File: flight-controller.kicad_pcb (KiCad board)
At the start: 2 copper layers, 36 x 36 mm, 9 parts, among them J1 USB_C_Receptacle_USB2.0, U1 AT32F435RGT7, U2 BMI270, U3 BMP280, U4 W25N01GVZEIG, U5 AT7456E, U6 TPS54335A, U7 TPS54335A, U8 TLV75733PDBV

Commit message: Finish majority of MCU pin mapping
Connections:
- U1 pad 10: unconnected-(U1-PC2-Pad10) -> TMR20_CH2
- U1 pad 20: unconnected-(U1-PA4-Pad20) -> SPI1_CS
- U1 pad 24: unconnected-(U1-PC4-Pad24) -> TMR9_CH1
- U1 pad 25: unconnected-(U1-PC5-Pad25) -> TMR9_CH2
- U1 pad 26: unconnected-(U1-PB0-Pad26) -> SPI1_INT
- U1 pad 29: unconnected-(U1-PB10-Pad29) -> TMR2_CH3
- U1 pad 30: unconnected-(U1-PB11-Pad30) -> TMR2_CH4
- U1 pad 33: unconnected-(U1-PB12-Pad33) -> SPI2_CS
- U1 pad 37: unconnected-(U1-PC6-Pad37) -> TIM3_CH1
- U1 pad 38: unconnected-(U1-PC7-Pad38) -> TIM3_CH2
- U1 pad 39: unconnected-(U1-PC8-Pad39) -> TIM3_CH3
- U1 pad 40: unconnected-(U1-PC9-Pad40) -> TIM3_CH4
- U1 pad 54: unconnected-(U1-PD2-Pad54) -> SPI3_CS
- U1 pad 58: unconnected-(U1-PB6-Pad58) -> SPI4_CS
- U1 pad 8: unconnected-(U1-PC0-Pad8) -> I2C3_SCL
- U1 pad 9: unconnected-(U1-PC1-Pad9) -> I2C3_SDA
- U2 pad 12: unconnected-(U2-CSB-Pad12) -> SPI1_CS
- U2 pad 4: unconnected-(U2-INT1-Pad4) -> SPI1_INT
- U3 pad 2: unconnected-(U3-CSB-Pad2) -> SPI2_CS
- U4 pad 1: unconnected-(U4-~{CS}-Pad1) -> SPI3_CS
- U4 pad 4: unconnected-(U4-GND-Pad4) -> GND
- U4 pad 8: unconnected-(U4-VCC-Pad8) -> +3V3
- U4 pad 9: unconnected-(U4-EP-Pad9) -> GND
- U5 pad 20: unconnected-(U5-AGND-Pad20) -> GND
- U5 pad 21: unconnected-(U5-AVDD-Pad21) -> +5V
- U5 pad 23: unconnected-(U5-PGND-Pad23) -> GND
- U5 pad 24: unconnected-(U5-PVDD-Pad24) -> +5V
- U5 pad 27: unconnected-(U5-EP-Pad27) -> GND
- U5 pad 3: unconnected-(U5-DVDD-Pad3) -> +5V
- U5 pad 4: unconnected-(U5-DGND-Pad4) -> GND
- U5 pad 8: unconnected-(U5-~{CS}-Pad8) -> SPI4_CS
- U8 pad 1: unconnected-(U8-IN-Pad1) -> +5V
- U8 pad 2: unconnected-(U8-GND-Pad2) -> GND
- U8 pad 5: unconnected-(U8-OUT-Pad5) -> +3V3

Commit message: Update pcb to match minor schematic change
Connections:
- U1 pad 10: TMR20_CH2 -> unconnected-(U1-PC2-Pad10)
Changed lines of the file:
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@@
   (net 44 "unconnected-(U1-PH1-Pad6)")
   (net 45 "NRST")
-  (net 46 "TMR20_CH2")
+  (net 46 "unconnected-(U1-PC2-Pad10)")
   (net 47 "TMR9_CH1")
   (net 48 "TMR9_CH2")
@@
       (net 38 "I2C3_SDA") (pinfunction "PC1") (pintype "unspecified"))
     (pad "10" smd roundrect (at -5.675 0.75) (size 1.55 0.3) (layers "F.Cu" "F.Paste" "F.Mask") (roundrect_rratio 0.25)
-      (net 46 "TMR20_CH2") (pinfunction "PC2") (pintype "unspecified"))
+      (net 46 "unconnected-(U1-PC2-Pad10)") (pinfunction "PC2") (pintype "unspecified"))
     (pad "11" smd roundrect (at -5.675 1.25) (size 1.55 0.3) (layers "F.Cu" "F.Paste" "F.Mask") (roundrect_rratio 0.25)
       (net 49 "unconnected-(U1-PC3-Pad11)") (pinfunction "PC3") (pintype "unspecified"))

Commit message: Add buzzer and power supply designs for consideration
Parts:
- added U9: USBLC6-2P6, Package_TO_SOT_SMD:SOT-666, F.Cu at (109.8, 100.6)
- U6, U7: value TPS54335A -> TPS54302; footprint Package_SO:TI_SO-PowerPAD-8_ThermalVias -> Package_TO_SOT_SMD:SOT-23-6
- moved U7 3.03 mm to (105.2, 105.6)
- moved U6 2.71 mm to (105.2, 101.2)
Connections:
- net Net-(J1-VBUS-PadA4) renamed VBUS
- J1 pad A6: USB_DP -> EUSB_DP
- J1 pad A7: USB_DM -> EUSB_DM
- J1 pad B6: USB_DP -> EUSB_DP
- J1 pad B7: USB_DM -> EUSB_DM
- U2 pad 2: unconnected-(U2-ASDx-Pad2) -> +3V3
- U2 pad 3: unconnected-(U2-ASCx-Pad3) -> +3V3
- U6 pad 1: unconnected-(U6-BOOT-Pad1) -> GND
- U6 pad 2: unconnected-(U6-VIN-Pad2) -> Net-(U6-SW)
- U6 pad 3: unconnected-(U6-PH-Pad3) -> +BATT
- U6 pad 4: unconnected-(U6-GND-Pad4) -> Net-(U6-FB)
- U6 pad 6: unconnected-(U6-COMP-Pad6) -> Net-(U6-BOOT)
- U7 pad 1: unconnected-(U7-BOOT-Pad1) -> GND
- U7 pad 2: unconnected-(U7-VIN-Pad2) -> Net-(U7-SW)
- U7 pad 3: unconnected-(U7-PH-Pad3) -> +BATT
- U7 pad 4: unconnected-(U7-GND-Pad4) -> Net-(U7-FB)
- U7 pad 5: unconnected-(U7-VSENSE-Pad5) -> 10V_SW
- U7 pad 6: unconnected-(U7-COMP-Pad6) -> Net-(U7-BOOT)
- U8 pad 3: unconnected-(U8-EN-Pad3) -> +5V

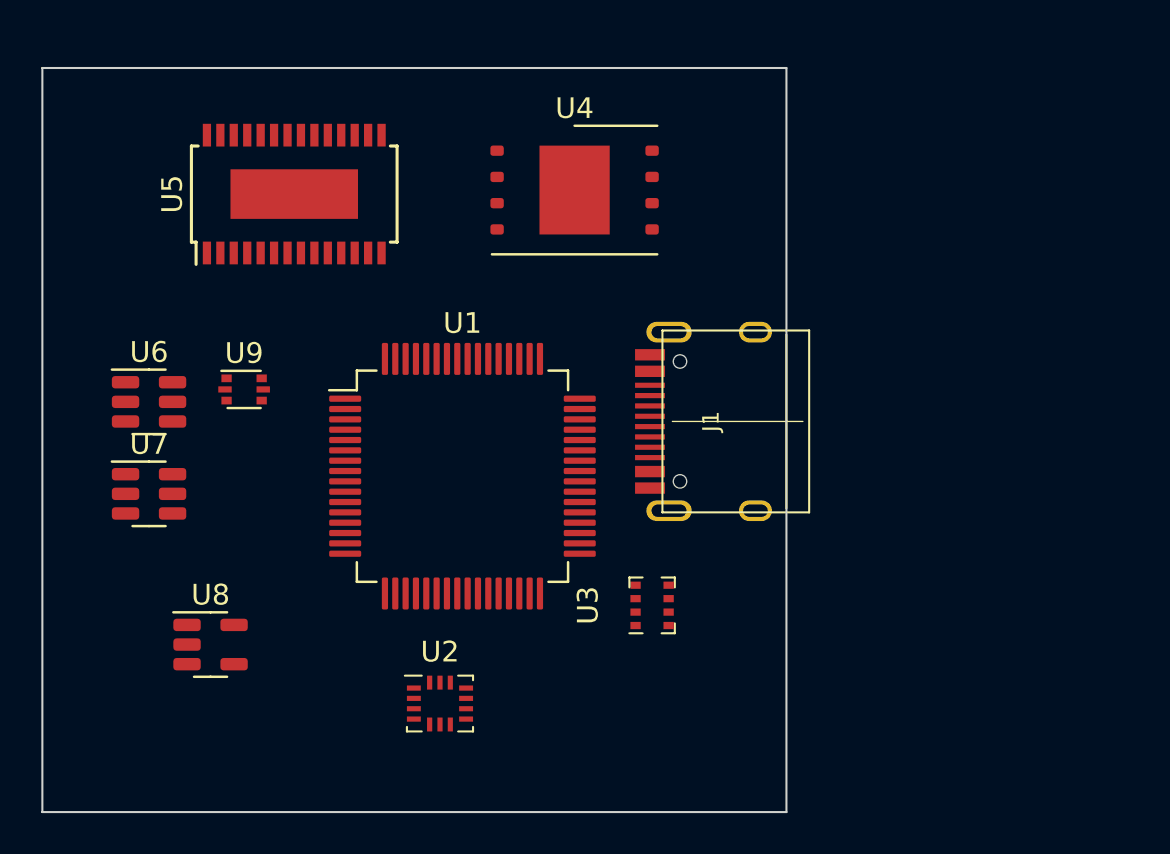
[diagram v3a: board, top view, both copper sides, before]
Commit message: Add LCSC part numbers for major parts. Provisionally delect power supply capacitors and inductors.
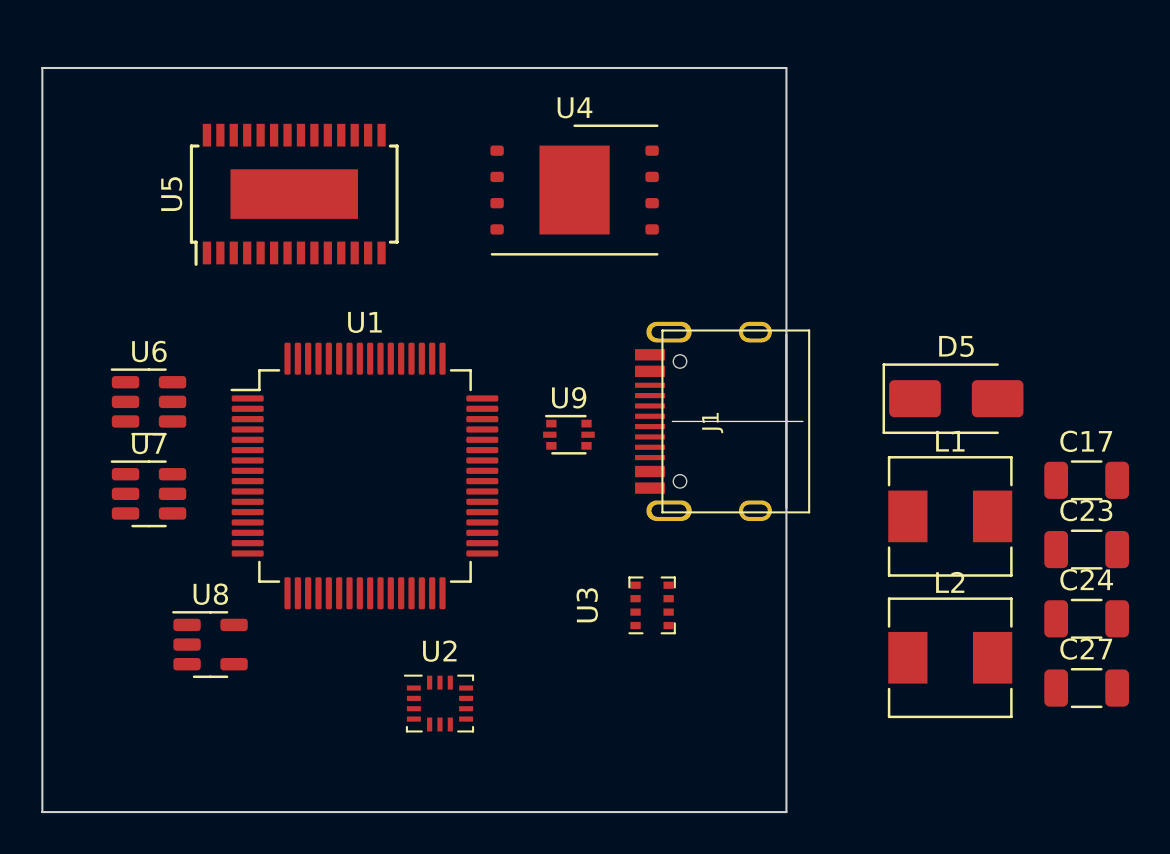
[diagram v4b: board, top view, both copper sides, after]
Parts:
- added C17: 22u, Capacitor_SMD:C_1206_3216Metric, F.Cu at (150.5, 105.0)
- added C23: 22u, Capacitor_SMD:C_1206_3216Metric, F.Cu at (150.5, 108.3)
- added C24: 22u, Capacitor_SMD:C_1206_3216Metric, F.Cu at (150.5, 111.7)
- added C27: 22u, Capacitor_SMD:C_1206_3216Metric, F.Cu at (150.5, 115.0)
- added D5: SS34, Diode_SMD:D_SMA, F.Cu at (144.2, 101.0)
- added L1: 10u, Inductor_SMD:L_Sunlord_MWSA0503S, F.Cu at (143.9, 106.7)
- added L2: 10u, Inductor_SMD:L_Sunlord_MWSA0503S, F.Cu at (143.9, 113.5)
- moved U9 15.9 mm to (125.5, 102.7)
- moved U1 4.72 mm to (115.6, 104.7)

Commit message: Add remaining OSD components
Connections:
- U5 pad 19: unconnected-(U5-~{RESET}-Pad19) -> +5V
- U5 pad 22: unconnected-(U5-VIN-Pad22) -> Net-(U5-VIN)
- U5 pad 25: unconnected-(U5-SAG-Pad25) -> Net-(U5-SAG)
- U5 pad 26: unconnected-(U5-VOUT-Pad26) -> Net-(U5-VOUT)
- U5 pad 5: unconnected-(U5-CLKIN-Pad5) -> Net-(U5-CLKIN)
- U5 pad 6: unconnected-(U5-XFB-Pad6) -> Net-(U5-XFB)

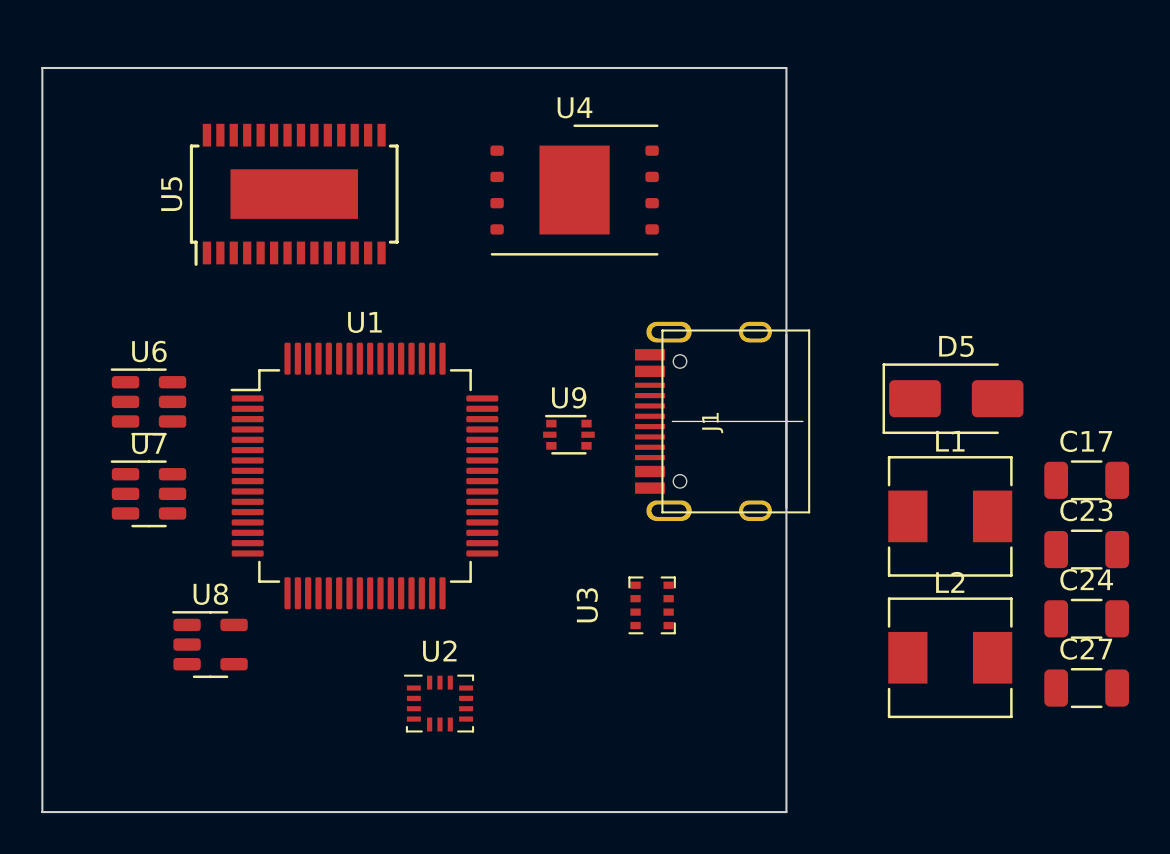
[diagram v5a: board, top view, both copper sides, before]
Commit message: Complete majority of component selection
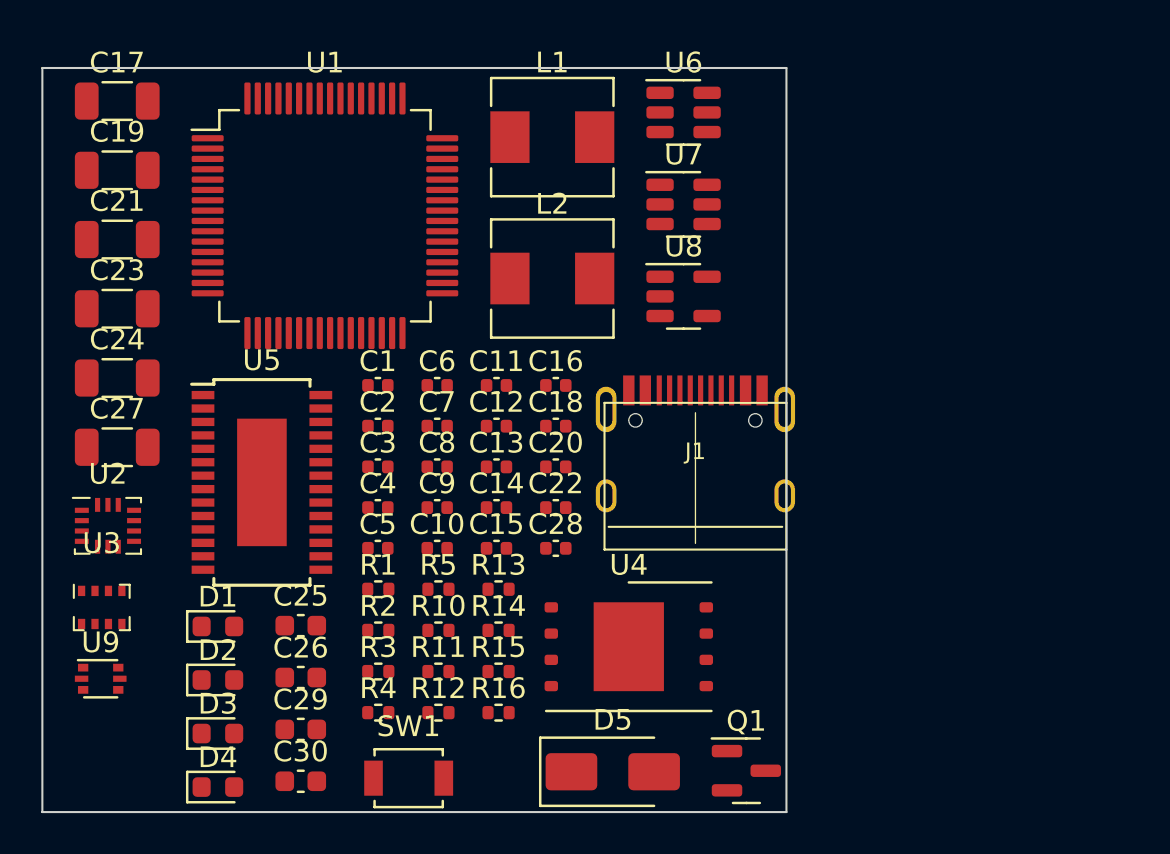
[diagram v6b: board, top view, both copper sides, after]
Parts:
- added C1: 100n, Capacitor_SMD:C_0402_1005Metric, F.Cu at (116.2, 100.4)
- added C10: 100n, Capacitor_SMD:C_0402_1005Metric, F.Cu at (119.1, 108.2)
- added C11: 100n, Capacitor_SMD:C_0402_1005Metric, F.Cu at (122.0, 100.4)
- added C12: 100n, Capacitor_SMD:C_0402_1005Metric, F.Cu at (122.0, 102.3)
- added C13: 100n, Capacitor_SMD:C_0402_1005Metric, F.Cu at (122.0, 104.3)
- added C14: 100n, Capacitor_SMD:C_0402_1005Metric, F.Cu at (122.0, 106.3)
- added C15: 100n, Capacitor_SMD:C_0402_1005Metric, F.Cu at (122.0, 108.2)
- added C16: 68p, Capacitor_SMD:C_0402_1005Metric, F.Cu at (124.8, 100.4)
- added C18: 100n, Capacitor_SMD:C_0402_1005Metric, F.Cu at (124.8, 102.3)
- added C19: 10u 50V, Capacitor_SMD:C_1206_3216Metric, F.Cu at (103.6, 90.0)
- added C2: 100n, Capacitor_SMD:C_0402_1005Metric, F.Cu at (116.2, 102.3)
- added C20: 100n, Capacitor_SMD:C_0402_1005Metric, F.Cu at (124.8, 104.3)
- added C21: 10u 50V, Capacitor_SMD:C_1206_3216Metric, F.Cu at (103.6, 93.3)
- added C22: 68p, Capacitor_SMD:C_0402_1005Metric, F.Cu at (124.8, 106.3)
- added C25: 10u, Capacitor_SMD:C_0603_1608Metric, F.Cu at (112.5, 112.0)
- added C26: 10u, Capacitor_SMD:C_0603_1608Metric, F.Cu at (112.5, 114.5)
- added C28: 100n, Capacitor_SMD:C_0402_1005Metric, F.Cu at (124.8, 108.2)
- added C29: 10u, Capacitor_SMD:C_0603_1608Metric, F.Cu at (112.5, 117.0)
- added C3: 100n, Capacitor_SMD:C_0402_1005Metric, F.Cu at (116.2, 104.3)
- added C30: 10u, Capacitor_SMD:C_0603_1608Metric, F.Cu at (112.5, 119.5)
- added C4: 100n, Capacitor_SMD:C_0402_1005Metric, F.Cu at (116.2, 106.3)
- added C5: 100n, Capacitor_SMD:C_0402_1005Metric, F.Cu at (116.2, 108.2)
- added C6: 100n, Capacitor_SMD:C_0402_1005Metric, F.Cu at (119.1, 100.4)
- added C7: 100n, Capacitor_SMD:C_0402_1005Metric, F.Cu at (119.1, 102.3)
- added C8: 100n, Capacitor_SMD:C_0402_1005Metric, F.Cu at (119.1, 104.3)
- added C9: 100n, Capacitor_SMD:C_0402_1005Metric, F.Cu at (119.1, 106.3)
- added D1: BLUE, LED_SMD:LED_0603_1608Metric, F.Cu at (108.5, 112.0)
- added D2: GREEN, LED_SMD:LED_0603_1608Metric, F.Cu at (108.5, 114.6)
- added D3: RED, LED_SMD:LED_0603_1608Metric, F.Cu at (108.5, 117.2)
- added D4: YELLOW, LED_SMD:LED_0603_1608Metric, F.Cu at (108.5, 119.8)
- added Q1: AO3400A, Package_TO_SOT_SMD:SOT-23, F.Cu at (134.1, 119.0)
- added R1: 10k, Resistor_SMD:R_0402_1005Metric, F.Cu at (116.3, 110.2)
- added R10: 100k, Resistor_SMD:R_0402_1005Metric, F.Cu at (119.2, 112.2)
- added R11: 6.34k, Resistor_SMD:R_0402_1005Metric, F.Cu at (119.2, 114.2)
- added R12: 100k, Resistor_SMD:R_0402_1005Metric, F.Cu at (119.2, 116.2)
- added R13: 13.3k, Resistor_SMD:R_0402_1005Metric, F.Cu at (122.1, 110.2)
- added R14: 10k, Resistor_SMD:R_0402_1005Metric, F.Cu at (122.1, 112.2)
- added R15: 75, Resistor_SMD:R_0402_1005Metric, F.Cu at (122.1, 114.2)
- added R16: 75, Resistor_SMD:R_0402_1005Metric, F.Cu at (122.1, 116.2)
- added R2: 5.1k, Resistor_SMD:R_0402_1005Metric, F.Cu at (116.3, 112.2)
- added R3: 5.1k, Resistor_SMD:R_0402_1005Metric, F.Cu at (116.3, 114.2)
- added R4: 10k, Resistor_SMD:R_0402_1005Metric, F.Cu at (116.3, 116.2)
- added R5: 10k, Resistor_SMD:R_0402_1005Metric, F.Cu at (119.2, 110.2)
- added SW1: SW_Push, Button_Switch_SMD:SW_SPST_B3U-1000P, F.Cu at (117.7, 119.4)
- moved C17 50.4 mm to (103.6, 86.6)
- moved C23 48.3 mm to (103.6, 96.7)
- moved C24 48.3 mm to (103.6, 100.0)
- moved C27 48.3 mm to (103.6, 103.3)
- moved U6 29.4 mm to (131.0, 87.2)
- moved U7 29.4 mm to (131.0, 91.6)
- moved U8 28.4 mm to (131.0, 96.0)
- moved U3 26.6 mm to (102.9, 111.1), turned to 0 degrees
- moved L1 26.6 mm to (124.7, 88.3)
- moved L2 26.6 mm to (124.7, 95.2)
- moved U9 25.5 mm to (102.8, 114.5)
- moved D5 24.5 mm to (127.6, 119.0)
- moved U4 22.3 mm to (128.4, 113.0)
- moved U2 18.2 mm to (103.2, 107.2)
- moved U5 14.0 mm to (110.6, 105.0), turned to 0 degrees
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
